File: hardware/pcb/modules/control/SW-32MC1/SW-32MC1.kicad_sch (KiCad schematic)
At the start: 11 parts

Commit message: update dru
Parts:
- removed SW?: RotaryEncoder_Switch, symbol Device:RotaryEncoder_Switch
- added C1, C2, C3: 10nF, Capacitor_SMD:C_0603_1608Metric, symbol Device:C_Small
- added R1, R2: NC, Resistor_SMD:R_0603_1608Metric, symbol Device:R
- added R3: 10K, Resistor_SMD:R_0603_1608Metric, symbol Device:R
- added SW1: PEC11R-4225F-50024, SaawLib:Rotary_Encoder_Switched_PEC11R, symbol Device:RotaryEncoder_Switch
- RV1, RV2, RV3, RV4: renamed from RV?; footprint (none) -> Potentiometer_THT:Potentiometer_Bourns_PTV09A-1_Single_Vertical
- SW2, SW3: renamed from SW?; footprint (none) -> Button_Switch_SMD:SW_Push_1P1T_NO_6x6mm_H9.5mm
- gave numbers to parts that had none: 4
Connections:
- net BTN1 is gone; now on net SW1: R4.1, SW2.2
- net BTN2 is gone; now on net SW2: R5.1, SW3.2
- net CHA_LVL is gone; now on net LVL_A: RV1.2
- net CHB_LVL is gone; now on net LVL_B: RV2.2
- net CHC_LVL is gone; now on net LVL_C: RV3.2
- net CHD_LVL is gone; now on net LVL_D: RV4.2
- net +3V3: now also J1.2 (Pin_2), J2.2 (VCC), R1.1, R2.1, R3.1
- net GND: now also J1.1 (Pin_1), J2.1 (GND), C1.2, C2.2, C3.2, SW1.C, SW1.S2
- net SCL: now reaches J2.3 (SCL)
- net SCL: now also J1.3 (Pin_3)
- net SDA: now reaches J2.4 (SDA)
- net SDA: now also J1.4 (Pin_4)
- net LVL_A: now reaches J1.10 (Pin_10)
- net LVL_B: now reaches J1.11 (Pin_11)
- net LVL_C: now reaches J1.12 (Pin_12)
- net LVL_D: now reaches J1.13 (Pin_13)
- net ENC_A: now reaches J1.5 (Pin_5)
- net ENC_A: now also C2.1, R2.2, SW1.A
- net ENC_B: now reaches J1.6 (Pin_6)
- net ENC_B: now also C1.1, R1.2, SW1.B
- net ENC_SW: now reaches J1.7 (Pin_7)
- net ENC_SW: now also C3.1, R3.2, SW1.S1
- net SW1: now reaches J1.8 (Pin_8)
- net SW2: now reaches J1.9 (Pin_9)
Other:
- note added: "1.5" OLED Module"
- note added: "Rotary Encoder"
- moved on the sheet: J1, J2, R4, R5, RV1, RV2, RV3, RV4, SW2, SW3

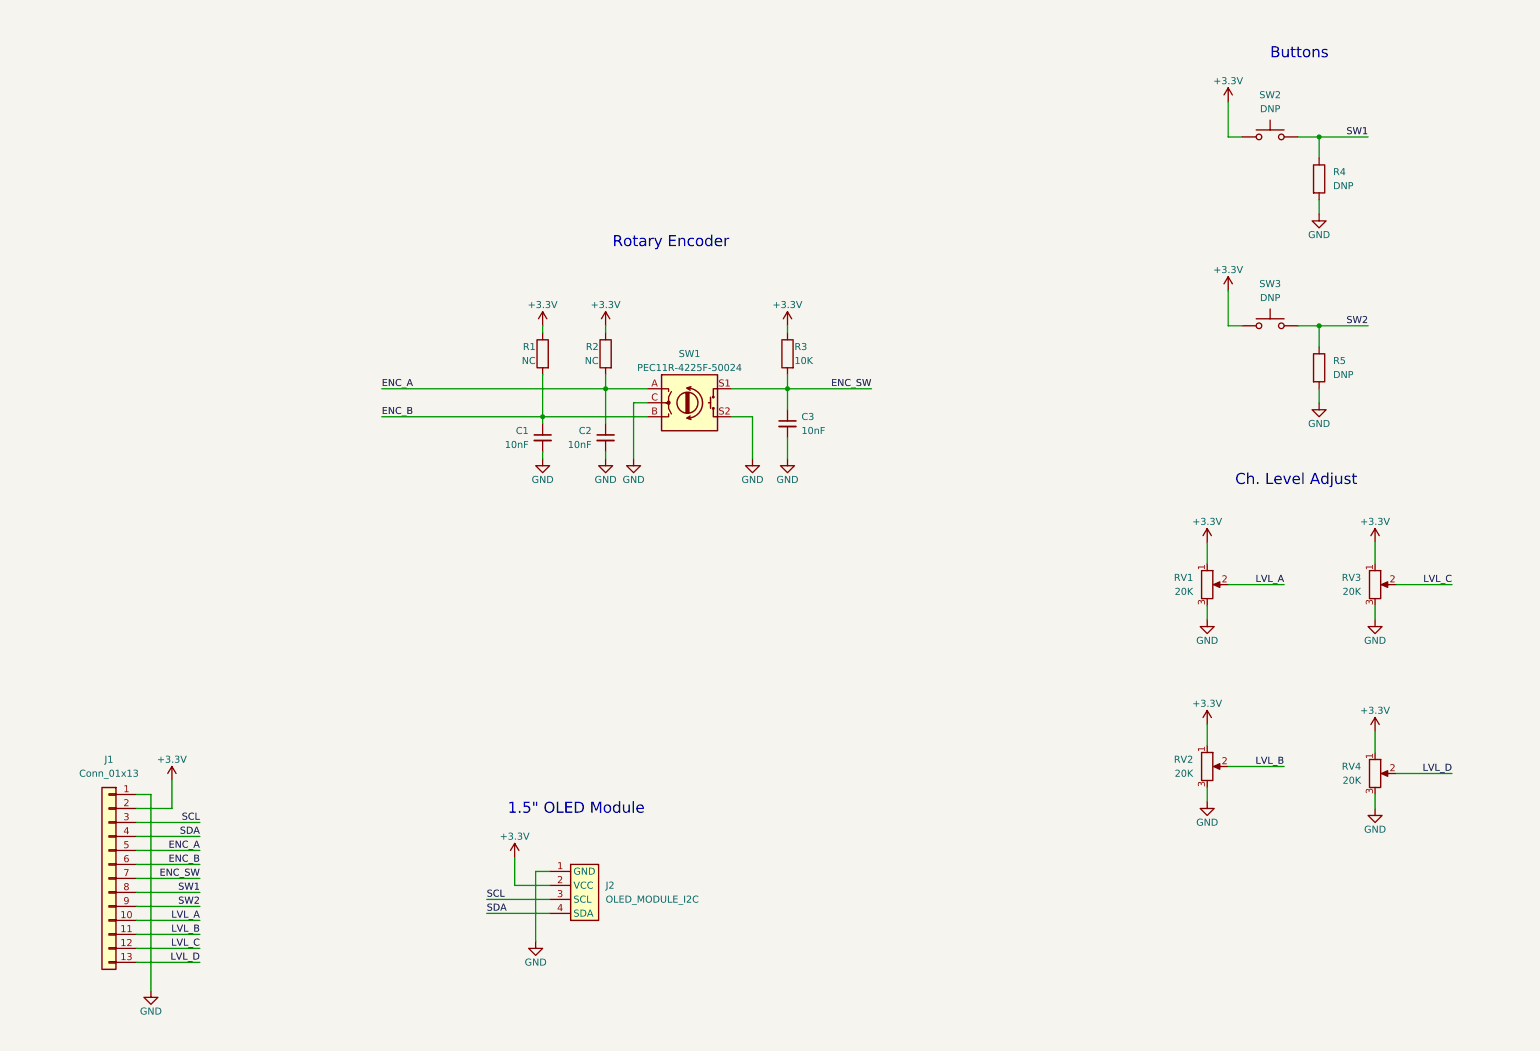
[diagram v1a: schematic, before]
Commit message: add main mcu to front panel
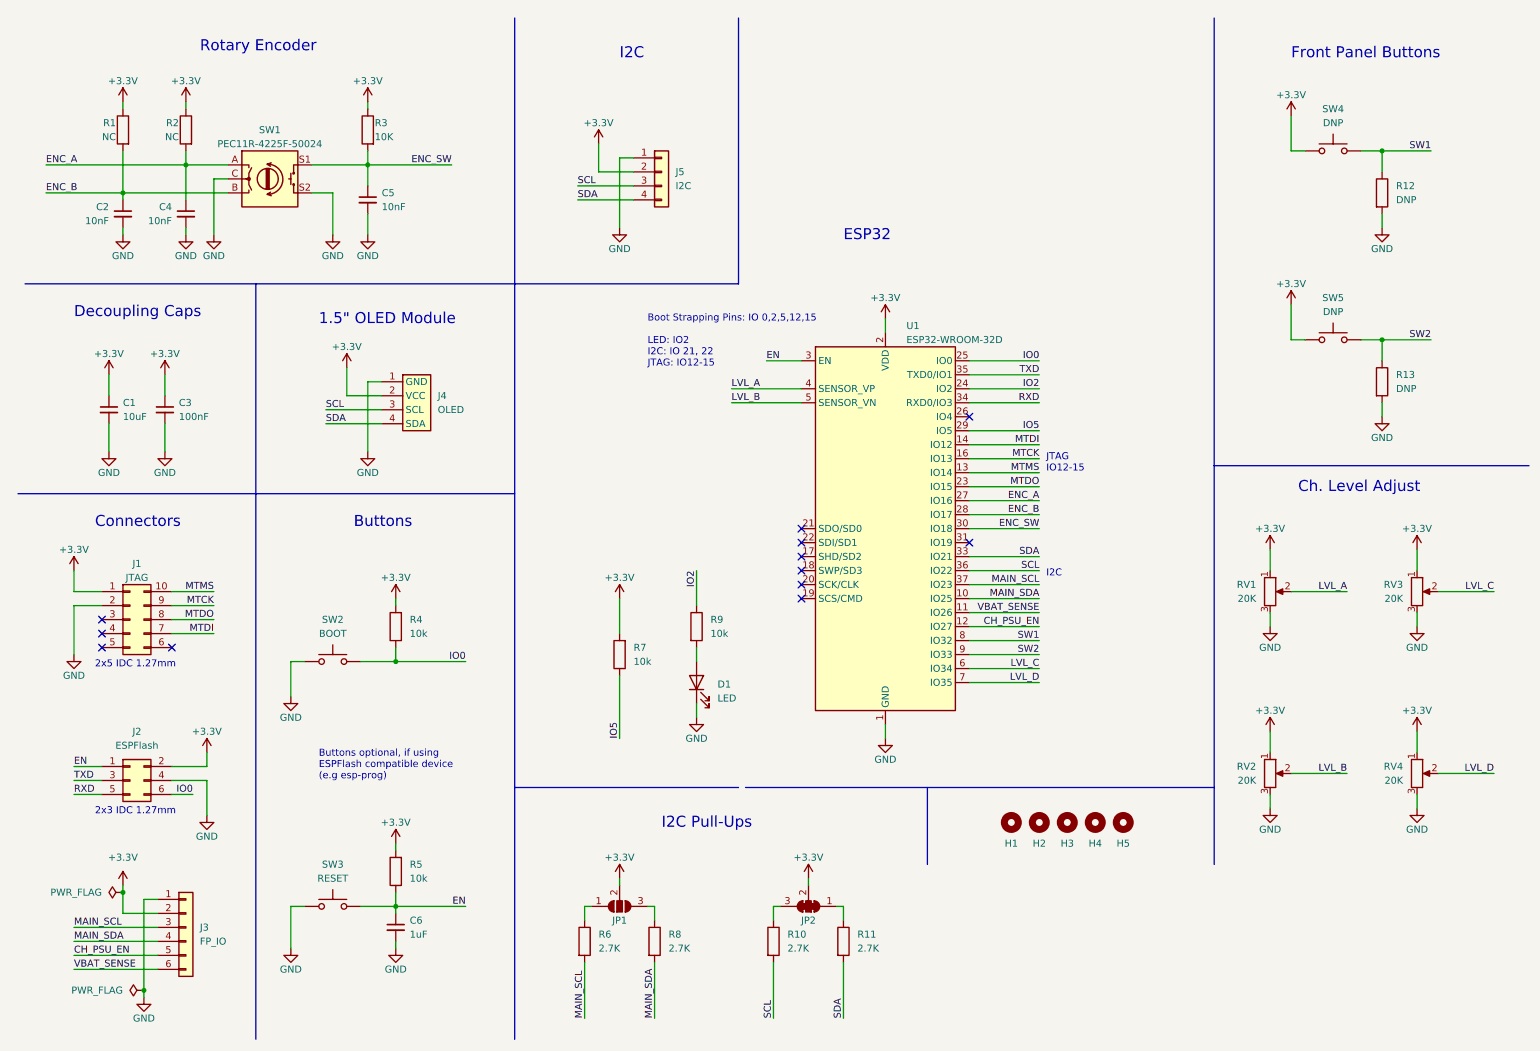
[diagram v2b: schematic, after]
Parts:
- removed J1: Conn_01x13, symbol Connector_Generic:Conn_01x13
- removed J2: OLED_MODULE_I2C, SaawLib:OLED_I2C, symbol SaawLib:OLED_MODULE_I2C
- added C1: 10uF, Capacitor_SMD:C_0603_1608Metric, symbol Device:C_Small
- added C3: 100nF, Capacitor_SMD:C_0603_1608Metric, symbol Device:C_Small
- added C6: 1uF, Capacitor_SMD:C_0603_1608Metric, symbol Device:C_Small
- added D1: LED, symbol Device:LED
- added H1, H2, H3, H4, H5: MountingHole, MountingHole:MountingHole_2.2mm_M2, symbol Mechanical:MountingHole
- added J1: JTAG, Connector_PinHeader_1.27mm:PinHeader_2x05_P1.27mm_Vertical, symbol Connector_Generic:Conn_02x05_Counter_Clockwise
- added J2: ESPFlash, Connector_PinHeader_1.27mm:PinHeader_2x03_P1.27mm_Vertical, symbol Connector_Generic:Conn_02x03_Odd_Even
- added J3: FP_IO, symbol Connector_Generic:Conn_01x06
- added J4: OLED, SaawLib:OLED_I2C, symbol SaawLib:OLED_MODULE_I2C
- added J5: I2C, symbol Connector_Generic:Conn_01x04
- added JP1: SolderJumper_3_Open, symbol Jumper:SolderJumper_3_Open
- added JP2: SolderJumper_3_Bridged123, SaawLib:SolderJumper-3_P1.3mm_Bridged123_Pad1.0x1.5mm_NumberLabels, symbol Jumper:SolderJumper_3_Bridged123
- added R10, R11, R6, R8: 2.7K, Resistor_SMD:R_0603_1608Metric, symbol Device:R
- added R4, R5, R7, R9: 10k, Resistor_SMD:R_0603_1608Metric, symbol Device:R
- added SW2: BOOT, Button_Switch_SMD:SW_Push_SPST_NO_Alps_SKRK, symbol Switch:SW_Push
- added SW3: RESET, Button_Switch_SMD:SW_Push_SPST_NO_Alps_SKRK, symbol Switch:SW_Push
- added U1: ESP32-WROOM-32D, RF_Module:ESP32-WROOM-32, symbol RF_Module:ESP32-WROOM-32D
- renumbered C1 to C2, C2 to C4, C3 to C5, R4 to R12, R5 to R13, SW2 to SW4, SW3 to SW5
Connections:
- net +3V3: now also C1.1, C3.1, J1.1 (Pin_1), J2.2 (Pin_2), J3.2 (Pin_2), J4.2 (VCC), J5.2 (Pin_2), JP1.2 (C), JP2.2 (C), R4.2, R5.2, R7.2, U1.2 (VDD)
- net ENC_A: now also U1.27 (IO16)
- net ENC_B: now also U1.28 (IO17)
- net ENC_SW: now also U1.30 (IO18)
- net GND: now also C1.2, C3.2, C6.2, D1.1 (K), J1.2 (Pin_2), J2.4 (Pin_4), J3.1 (Pin_1), J4.1 (GND), J5.1 (Pin_1), SW2.1, SW3.1, U1.1 (GND), U1.15 (GND), U1.38 (GND), U1.39 (GND)
- net LVL_A: now also U1.4 (SENSOR_VP)
- net LVL_B: now also U1.5 (SENSOR_VN)
- net LVL_C: now also U1.6 (IO34)
- net LVL_D: now also U1.7 (IO35)
- net SCL: now also J4.3 (SCL), J5.3 (Pin_3), R10.2, U1.36 (IO22)
- net SDA: now also J4.4 (SDA), J5.4 (Pin_4), R11.2, U1.33 (IO21)
- net SW1: now also U1.8 (IO32)
- net SW2: now also U1.9 (IO33)
- new net: JP2.1 (A), R11.1
- new net: JP1.3 (B), R8.1
- new net: JP2.3 (B), R10.1
- new net: JP1.1 (A), R6.1
- new net: D1.2 (A), R9.2
- new net CH_PSU_EN: J3.5 (Pin_5), U1.12 (IO27)
- new net EN: C6.1, J2.1 (Pin_1), R5.1, SW3.2, U1.3 (EN)
- new net IO0: J2.6 (Pin_6), R4.1, SW2.2, U1.25 (IO0)
- new net IO2: R9.1, U1.24 (IO2)
- new net IO5: R7.1, U1.29 (IO5)
- new net MAIN_SCL: J3.3 (Pin_3), R6.2, U1.37 (IO23)
- new net MAIN_SDA: J3.4 (Pin_4), R8.2, U1.10 (IO25)
- new net MTCK: J1.9 (Pin_9), U1.16 (IO13)
- new net MTDI: J1.7 (Pin_7), U1.14 (IO12)
- new net MTDO: J1.8 (Pin_8), U1.23 (IO15)
- new net MTMS: J1.10 (Pin_10), U1.13 (IO14)
- new net RXD: J2.5 (Pin_5), U1.34 (RXD0/IO3)
- new net TXD: J2.3 (Pin_3), U1.35 (TXD0/IO1)
- new net VBAT_SENSE: J3.6 (Pin_6), U1.11 (IO26)
- no-connect marks 0 -> 12
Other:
- note added: "2x3 IDC 1.27mm"
- note added: "2x5 IDC 1.27mm"
- note added: "Boot Strapping Pins: IO 0,2,5,12,15 LED: IO2 I2C: IO 21, 22 JTAG: IO12-15"
- note added: "Buttons optional, if using ESPFlash compatible device (e.g esp-prog)"
- note added: "Connectors"
- note added: "Decoupling Caps"
- note added: "ESP32"
- note added: "Front Panel Buttons"
- note added: "I2C"
- note added: "I2C Pull-Ups"
- note added: "JTAG IO12-15"
- moved on the sheet: C2, C4, C5, R1, R12, R13, R2, R3, RV1, RV2, RV3, RV4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

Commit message: update pdf
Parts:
- J1: footprint Connector_PinHeader_1.27mm:PinHeader_2x05_P1.27mm_Vertical -> Connector_PinHeader_2.54mm:PinHeader_2x05_P2.54mm_Vertical; symbol Connector_Generic:Conn_02x05_Counter_Clockwise -> Connector_Generic:Conn_02x05_Odd_Even
- J2: footprint Connector_PinHeader_1.27mm:PinHeader_2x03_P1.27mm_Vertical -> Connector_PinHeader_2.54mm:PinHeader_2x03_P2.54mm_Vertical
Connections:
- net GND: now also J1.3 (Pin_3); no longer J1.2 (Pin_2)
- net MTCK: now also J1.4 (Pin_4); no longer J1.9 (Pin_9)
- net MTDI: now also J1.8 (Pin_8); no longer J1.7 (Pin_7)
- net MTDO: now also J1.6 (Pin_6); no longer J1.8 (Pin_8)
- net MTMS: now also J1.2 (Pin_2); no longer J1.10 (Pin_10)
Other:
- note added: "2x3 IDC 2.54mm"
- note added: "2x5 IDC 2.54mm"
- note removed: "2x3 IDC 1.27mm"
- note removed: "2x5 IDC 1.27mm"
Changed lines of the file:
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@@
     (effects (font (size 1.27 1.27)) (justify left bottom))
   )
-  (text "2x5 IDC 1.27mm" (at 25.4 130.81 0)
+  (text "2x5 IDC 2.54mm" (at 25.4 130.81 0)
     (effects (font (size 1.27 1.27)) (justify left bottom))
   )
@@
     (effects (font (size 2 2)) (justify left bottom))
   )
-  (text "2x3 IDC 1.27mm" (at 25.4 157.48 0)
+  (text "2x3 IDC 2.54mm" (at 25.4 157.48 0)
     (effects (font (size 1.27 1.27)) (justify left bottom))
   )
@@
     (pin "2")
   )
-  (symbol (lib_id "Connector_Generic:Conn_02x05_Counter_Clockwise") (at 31.75 121.92 0) (unit 1)
+  (symbol (lib_id "Connector_Generic:Conn_02x05_Odd_Even") (at 31.75 121.92 0) (unit 1)
     (in_bom yes) (on_board yes)
     (property "Reference" "J1" (id 0) (at 33.02 111.76 0))
     (property "Value" "JTAG" (id 1) (at 33.02 114.3 0))
-    (property "Footprint" "Connector_PinHeader_1.27mm:PinHeader_2x05_P1.27mm_Vertical" (id 2) (at 31.75 121.92 0)
+    (property "Footprint" "Connector_PinHeader_2.54mm:PinHeader_2x05_P2.54mm_Vertical" (id 2) (at 31.75 121.92 0)
       (effects (font (size 1.27 1.27)) hide)
     )
@@
     (property "Reference" "J2" (id 0) (at 33.02 142.24 0))
     (property "Value" "ESPFlash" (id 1) (at 33.02 144.78 0))
-    (property "Footprint" "Connector_PinHeader_1.27mm:PinHeader_2x03_P1.27mm_Vertical" (id 2) (at 31.75 151.13 0)
+    (property "Footprint" "Connector_PinHeader_2.54mm:PinHeader_2x03_P2.54mm_Vertical" (id 2) (at 31.75 151.13 0)
       (effects (font (size 1.27 1.27)) hide)
     )
@@
     )
     (path "/194ffc13-377a-4b2f-81f5-2f5c9497fb3d"
-      (reference "J1") (unit 1) (value "JTAG") (footprint "Connector_PinHeader_1.27mm:PinHeader_2x05_P1.27mm_Vertical")
+      (reference "J1") (unit 1) (value "JTAG") (footprint "Connector_PinHeader_2.54mm:PinHeader_2x05_P2.54mm_Vertical")
     )
     (path "/f477751a-ac96-4d1d-a83a-b7186b62b616"
-      (reference "J2") (unit 1) (value "ESPFlash") (footprint "Connector_PinHeader_1.27mm:PinHeader_2x03_P1.27mm_Vertical")
+      (reference "J2") (unit 1) (value "ESPFlash") (footprint "Connector_PinHeader_2.54mm:PinHeader_2x03_P2.54mm_Vertical")
     )
     (path "/7e771610-b939-46e9-b4ba-d583d22aad23"

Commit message: many changes
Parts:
- removed R4, R5: 10k, Resistor_SMD:R_0603_1608Metric, symbol Device:R
- removed SW2: BOOT, Button_Switch_SMD:SW_Push_SPST_NO_Alps_SKRK, symbol Switch:SW_Push
- removed SW3: RESET, Button_Switch_SMD:SW_Push_SPST_NO_Alps_SKRK, symbol Switch:SW_Push
- added BZ1: Buzzer, symbol Device:Buzzer
- added C10, C11, C12, C7, C8, C9: 100nF, symbol Device:C_Small
- added D2: D_Small, symbol Device:D_Small
- added D3, D4, D5, D6, D7, D8: WS2812D, symbol LED:WS2812B
- added J3: FP_5V, Connector_JST:JST_XH_B2B-XH-A_1x02_P2.50mm_Vertical, symbol Connector_Generic:Conn_01x02
- added J6: RESET/FLASH, Connector_PinHeader_2.54mm:PinHeader_2x02_P2.54mm_Vertical, symbol Connector_Generic:Conn_02x02_Odd_Even
- added Q1: Q_NMOS_DGS, symbol Device:Q_NMOS_DGS
- added R10, R12: 10k, Resistor_SMD:R_0603_1608Metric, symbol Device:R
- added R11: 10, symbol Device:R
- added R13: 10K, symbol Device:R
- added R14: 100, symbol Device:R
- renumbered J3 to J4, J4 to J5, J5 to J7, JP2 to JP1, JP1 to JP2, R12 to R15, R13 to R16, R10 to R3, R6 to R4, R3 to R5, R11 to R6, R8 to R7, R7 to R8, SW4 to SW2, SW5 to SW3
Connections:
- net +3V3: now also BZ1.1 (-), D2.1 (K), R10.2, R12.2
- net EN: now also J6.2 (Pin_2), R12.1
- net GND: now also C10.1, C11.1, C12.1, C7.1, C8.1, C9.1, D3.3 (VSS), D4.3 (VSS), D5.3 (VSS), D6.3 (VSS), D7.3 (VSS), D8.3 (VSS), J3.2 (Pin_2), J6.1 (Pin_1), J6.3 (Pin_3), Q1.3 (S), R13.2
- net IO0: now also J6.4 (Pin_4), R10.1
- net LED_DATA: now reaches U1.26 (IO4)
- net LED_DATA: now also R14.1
- net BUZZER: now reaches U1.31 (IO19)
- net BUZZER: now also R11.1
- new net: D3.4 (DIN), R14.2
- new net: D7.2 (DOUT), D8.4 (DIN)
- new net: D6.2 (DOUT), D7.4 (DIN)
- new net: BZ1.2 (+), D2.2 (A), Q1.1 (D)
- new net: Q1.2 (G), R11.2, R13.1
- new net: D5.2 (DOUT), D6.4 (DIN)
- new net: D4.2 (DOUT), D5.4 (DIN)
- new net: D3.2 (DOUT), D4.4 (DIN)
- new net +5V: C10.2, C11.2, C12.2, C7.2, C8.2, C9.2, D3.1 (VDD), D4.1 (VDD), D5.1 (VDD), D6.1 (VDD), D7.1 (VDD), D8.1 (VDD), J3.1 (Pin_1)
- no-connect marks 12 -> 11
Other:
- note added: "Buzzer"
- note added: "DNP"
- note added: "Manual Reset/Boot"
- note added: "Pin header for manually resetting/flashing the ESP-32. Not needed, if using an ESPFlash compatible device (e.g esp-prog)."
- note added: "Status LEDs"
- note removed: "Buttons"
- note removed: "Buttons optional, if using ESPFlash compatible device (e.g esp-prog)"
- moved on the sheet: C1, C3, D1, J1, J2, J4, JP1, JP2, R3, R4, R6, R7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
